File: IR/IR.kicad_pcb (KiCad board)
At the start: 2 copper layers, 209 parts, among them J1 Conn_01x02_Male, J2 Conn_01x10_Female, J3 Conn_01x04_Male, J4 Conn_01x04_Male, Q1 SSM3J332R, Q10 SSM3J332R, Q11 2PB709AR, Q12 2PB709AR, Q13 SSM6K819R, Q14 SSM6K819R, Q15 SSM6K819R, Q16 SSM6K819R, Q2 BSS138, Q3 SSM3J332R, Q4 SSM3J332R, Q5 2PB709AR, Q6 SSM3J332R, Q7 2PB709AR, Q8 SSM3J332R, Q9 2PB709AR, SW1 SW_DIP_x05, SW2 SW_SPDT, SW4 SW_SPST, U1 TSSP58038, U10 TSSP58038, U11 TSSP58038, U12 TSSP58038, U13 TSSP58038, U14 TSSP58038, U15 TSSP58038, U16 TSSP58038, U17 TSSP58038, U18 74HC4051, U19 74HC4051, U2 TSSP58038, U20 STM32C031K4T6, U21 MAX3485, U3 TSSP58038, U4 TSSP58038, U5 AZ1084CD-3.3, U6 TSSP58038, U7 TSSP58038, U8 TSSP58038, U9 TSSP58038

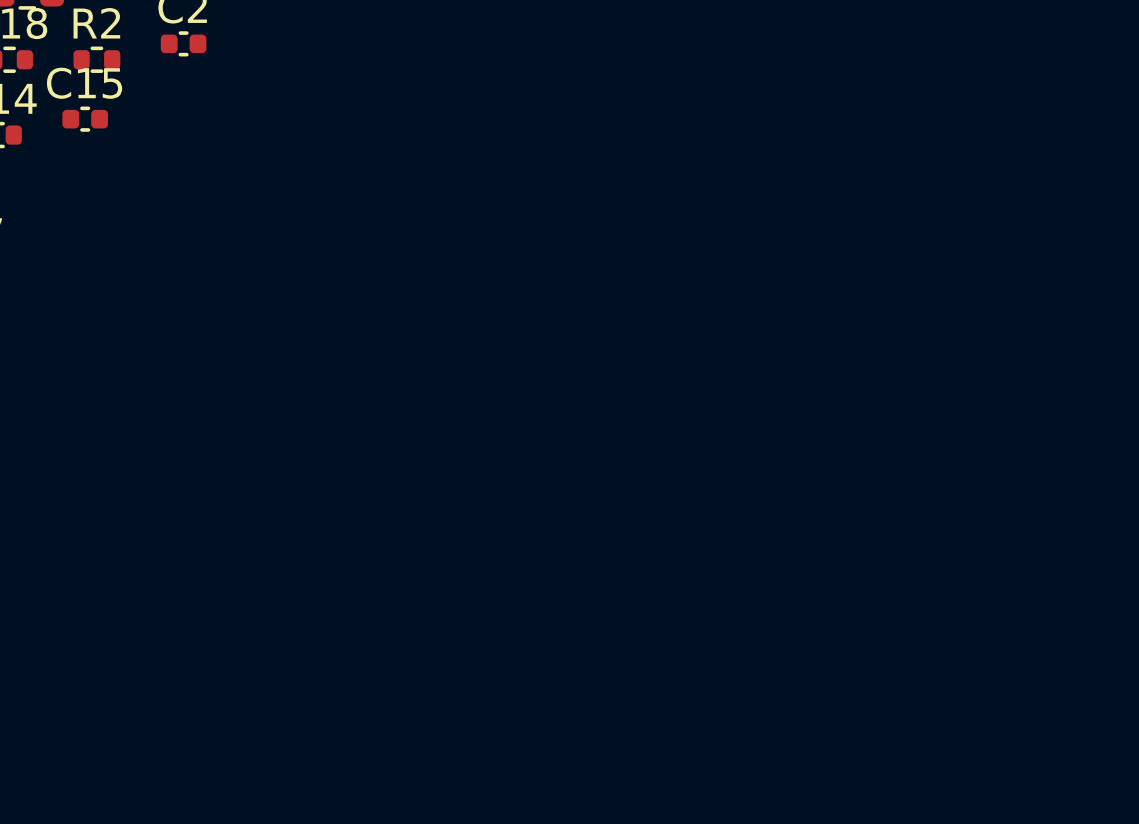
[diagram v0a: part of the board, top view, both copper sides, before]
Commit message: 構成図追加
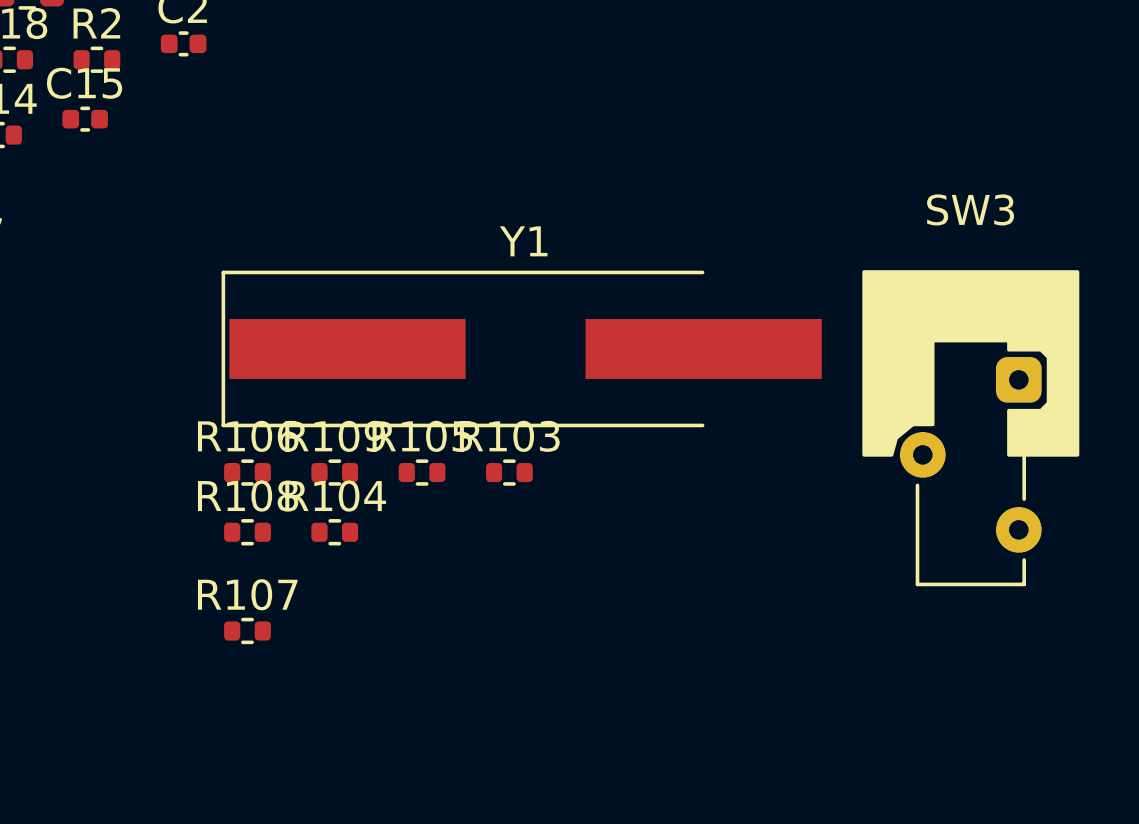
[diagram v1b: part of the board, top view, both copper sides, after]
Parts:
- added R103: 5.1k, Resistor_SMD:R_0402_1005Metric, F.Cu at (168.5, 62.2)
- added R104: 5.1k, Resistor_SMD:R_0402_1005Metric, F.Cu at (162.7, 64.2)
- added R105: 5.1k, Resistor_SMD:R_0402_1005Metric, F.Cu at (165.6, 62.2)
- added R106: 10k, Resistor_SMD:R_0402_1005Metric, F.Cu at (159.8, 62.2)
- added R107: 10k, Resistor_SMD:R_0402_1005Metric, F.Cu at (159.8, 67.5)
- added R108: 10k, Resistor_SMD:R_0402_1005Metric, F.Cu at (159.8, 64.2)
- added R109: 10k, Resistor_SMD:R_0402_1005Metric, F.Cu at (162.7, 62.2)
- added SW3: SW_SPDT_White, Slide_Switch:SW_Slide_SPDT_White, F.Cu at (183.9, 61.7)
- added Y1: 48MHz, Crystal:Crystal_SMD_HC49-SD_HandSoldering, F.Cu at (169.0, 58.1)
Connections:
- R32 pad 1: Mux_OUT0 -> GND
- R32 pad 2: GND -> Mux_OUT0
- R33 pad 1: Mux_OUT1 -> GND
- R33 pad 2: GND -> Mux_OUT1

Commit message: 人力曲面配線中
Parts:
- removed C24: 22pF, Capacitor_SMD:C_0603_1608Metric
- added C30: 0.1uF, Capacitor_SMD:C_0402_1005Metric, B.Cu at (119.5, 113.2)
- added C31: 0.1uF, Capacitor_SMD:C_0402_1005Metric, B.Cu at (120.2, 121.2)
- added U22: NJU6319AE, Package_SO:SOP-8_3.9x4.9mm_P1.27mm, B.Cu at (136.0, 102.8)
- C1, C14: value 4.7uF -> 1uF; footprint Capacitor_SMD:C_0603_1608Metric -> Capacitor_SMD:C_0402_1005Metric; moved to B.Cu
- C10, C11, C12, C13, C15, C16, C17, C18, C19, C2, C20, C21, C22, C25, C26, C29, C3, C4, C5, C6, C7, C8, C9, D10, D11, D7, D8, D9, H1, H2, H3, JP1, Q1, Q10, Q2, Q3, Q4, Q6, Q8, R1, R10, R100, R101, R102, R103, R104, R105, R106, R107, R108, R109, R11, R12, R13, R14, R15, R16, R17, R18, R19, R2, R20, R21, R22, R23, R24, R25, R26, R27, R28, R29, R3, R30, R31, R32, R33, R34, R35, R36, R37, R38, R39, R4, R40, R41, R42, R43, R44, R45, R46, R47, R48, R49, R5, R50, R51, R52, R53, R54, R55, R56, R57, R58, R59, R6, R60, R61, R62, R63, R64, R65, R66, R67, R68, R69, R7, R70, R71, R72, R73, R74, R75, R76, R77, R78, R79, R8, R80, R81, R82, R83, R84, R85, R86, R87, R88, R89, R9, R90, R91, R92, R93, R94, R95, R96, R97, R98, R99, TP1, TP2, TP3, U18, U19, U20, U21, U5: moved to B.Cu
- C23: value 22pF -> 0.1uF; footprint Capacitor_SMD:C_0603_1608Metric -> Capacitor_SMD:C_0402_1005Metric; moved to B.Cu
- D1, D2: value SBR1A40SA -> 1N5819WS; footprint Diode_SMD:D_SMA_Handsoldering -> Diode_SMD:D_SOD-323_HandSoldering; moved to B.Cu
- D12, D13, D14, D15, D16, D17, D18, D19, D20, D21, D22, D23, D24, D25, D26, D27: footprint LED_THT:LED_D3.0mm_Horizontal_O1.27mm_Z2.0mm -> LED_3.0mm_Center:LED_D3.0mm_Horizontal_O1.27mm_Z2.0mm
- J1: footprint Connector_Molex:Molex_SPOX_5268-02A_1x02_P2.50mm_Horizontal -> Connector_Molex:Molex_SPOX_5267-02A_1x02_P2.50mm_Vertical; moved to B.Cu
- J2: value Conn_01x10_Female -> Conn_01x10_Male; footprint Connector_IDC:IDC-Header_2x05_P2.54mm_Horizontal -> BoxHeader_1.27mm:BoxHeader_2x05_P1.27mm_Vertical_SMD
- J3, J4: footprint Connector_Molex:Molex_SPOX_5268-04A_1x04_P2.50mm_Horizontal -> Connector_Molex:Molex_SPOX_5267-04A_1x04_P2.50mm_Vertical; moved to B.Cu
- Q11, Q12, Q5, Q7, Q9: value 2PB709AR -> S8050; footprint Package_TO_SOT_SMD:SC-59_Handsoldering -> Package_TO_SOT_SMD:SOT-23; moved to B.Cu
- Q13, Q14, Q15, Q16: value SSM6K819R -> SSM3K345R; footprint TSOP6F:SSM6J808R -> Package_TO_SOT_SMD:SOT-23W; moved to B.Cu
- Y1: value 48MHz -> 16MHz; footprint Crystal:Crystal_SMD_HC49-SD_HandSoldering -> Crystal:Crystal_SMD_3225-4Pin_3.2x2.5mm_HandSoldering; moved to B.Cu
- moved D24 227.9 mm to (-43.2, 8.57), turned to -78.75 degrees
- moved D21 224.1 mm to (-24.4, -36.6), turned to -146.25 degrees
- moved D23 220.9 mm to (-43.2, -8.60), turned to -101.25 degrees
- moved D22 217.4 mm to (-36.6, -24.5), turned to -123.75 degrees
- moved D26 208.5 mm to (-24.4, 36.6), turned to -33.75 degrees
- moved D25 205.5 mm to (-36.6, 24.4), turned to -56.25 degrees
- moved D20 200.8 mm to (-8.58, -43.2), turned to -168.75 degrees
- moved R74 198.7 mm to (-44.6, -7.25), turned to -101.25 degrees
- moved R85 197.2 mm to (-35.3, -25.4), turned to 56.25 degrees
- moved R82 197.1 mm to (-44.0, -10.2), turned to 78.75 degrees
- moved SW3 196.4 mm to (-11.5, 82.0)
- moved R77 195.2 mm to (-37.0, -22.9), turned to -123.75 degrees
- moved D19 194.6 mm to (8.58, -43.2), turned to 168.75 degrees
- moved R81 193.1 mm to (-36.5, -26.3), turned to 56.25 degrees
- moved R92 188.4 mm to (-38.4, 23.6), turned to 123.75 degrees
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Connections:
- C23 pad 1: GND -> +3.3V
- C23 pad 2: OSC_IN -> GND
- Q13 pad 1: IR_emit0 -> Blightness_Max
- Q13 pad 2: IR_emit0 -> GND
- Q13 pad 3: Blightness_Max -> IR_emit0
- Q14 pad 1: IR_emit1 -> Blightness_2nd
- Q14 pad 2: IR_emit1 -> GND
- Q14 pad 3: Blightness_2nd -> IR_emit1
- Q15 pad 1: IR_emit2 -> Blightness_3rd
- Q15 pad 2: IR_emit2 -> GND
- Q15 pad 3: Blightness_3rd -> IR_emit2
- Q16 pad 1: IR_emit3 -> Blightness_Min
- Q16 pad 2: IR_emit3 -> GND
- Q16 pad 3: Blightness_Min -> IR_emit3
- U20 pad 2: unconnected-(U20-Pad2) -> OSC_IN
- U20 pad 6: unconnected-(U20-Pad6) -> NRST
- Y1 pad 1: OSC_OUT -> Net-(U22-Pad2)
- Y1 pad 2: OSC_IN -> GND
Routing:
- net GND: track 0.00 -> 281.0 mm, vias 0 -> 4
- net +3.3V: track 0.00 -> 258.5 mm
- net IR_rcpt8: track 0.00 -> 112.6 mm
- net VDD: track 0.00 -> 98.5 mm
- net IR_rcpt7: track 0.00 -> 96.8 mm
- net IR_rcpt6: track 0.00 -> 80.2 mm
- net IR_rcpt5: track 0.00 -> 66.9 mm
- net IR_rcpt4: track 0.00 -> 59.0 mm
- net IR_rcpt3: track 0.00 -> 40.8 mm
- net IR_emit1: track 0.00 -> 39.6 mm
- net IR_rcpt2: track 0.00 -> 23.0 mm
- net IR_emit0: track 0.00 -> 21.5 mm
- net Net-(D19-Pad1): track 0.00 -> 6.99 mm
- net Net-(D20-Pad1): track 0.00 -> 5.73 mm
- net Net-(D18-Pad1): track 0.00 -> 5.06 mm
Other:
- board outline added: 96 x 138 mm

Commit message: ゴリ押し人力配線
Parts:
- moved U19 178.8 mm to (-41.5, 57.1), turned to -157.5 degrees
- moved C31 178.4 mm to (-46.3, 57.2), turned to -67.5 degrees
- moved C18 147.3 mm to (-39.1, -15.2), turned to 67.5 degrees
- moved C17 144.8 mm to (-30.4, -29.0), turned to 45 degrees
- moved C19 144.3 mm to (-41.9, 0.70), turned to 90 degrees
- moved C16 137.9 mm to (-16.9, -38.6), turned to 22.5 degrees
- moved C20 137.6 mm to (-38.4, 17.0), turned to 112.5 degrees
- moved C21 126.5 mm to (-29.1, 30.4), turned to 135 degrees
- moved C15 126.2 mm to (-0.79, -42.2), turned to 0 degrees
- moved C12 115.0 mm to (15.3, -39.4), turned to -22.5 degrees
- moved C22 111.9 mm to (-15.4, 39.2), turned to 157.5 degrees
- moved C11 97.9 mm to (29.3, -30.4), turned to -45 degrees
- moved C3 86.7 mm to (0.94, 42.2)
- moved C10 79.8 mm to (38.7, -16.9), turned to -67.5 degrees
- moved C4 70.7 mm to (17.0, 38.7), turned to -157.5 degrees
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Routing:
- net IR_emit2: track 0.00 -> 151.2 mm, vias 0 -> 13
- net IR_emit3: track 0.00 -> 140.8 mm, vias 0 -> 13
- net IR_emit1: track 39.6 -> 177.2 mm, vias 0 -> 13
- net IR_emit0: track 21.5 -> 130.8 mm
- net GND: track 281.0 -> 389.5 mm, vias 4 -> 26
- net IR_rcpt9: track 0.00 -> 98.5 mm
- net +3.3V: track 258.5 -> 356.0 mm
- net IR_rcpt10: track 0.00 -> 83.0 mm
- net IR_rcpt11: track 0.00 -> 69.5 mm
- net IR_rcpt12: track 0.00 -> 62.5 mm
- net IR_rcpt13: track 0.00 -> 51.0 mm
- net IR_rcpt14: track 0.00 -> 28.4 mm
- net IR_rcpt15: track 0.00 -> 12.7 mm
- net IR_rcpt6: track 80.2 -> 87.0 mm
- net IR_rcpt8: track 112.6 -> 118.8 mm
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
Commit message: IR半分
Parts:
- removed C13: ADJ_ST, Capacitor_SMD:C_0603_1608Metric
- removed C14: 1uF, Capacitor_SMD:C_0402_1005Metric
- removed C2: 0.1uF, Capacitor_SMD:C_0402_1005Metric
- removed D10, D9: Green, LED_SMD:LED_0603_1608Metric_Pad1.05x0.95mm_HandSolder
- removed D7: D_Zener, Diode_SMD:D_SOD-323_HandSoldering
- removed H1, H2: MountingHole_Pad, TestPoint:TestPoint_Pad_1.5x1.5mm
- removed Q10, Q4, Q6, Q8: SSM3J332R, Package_TO_SOT_SMD:SOT-23W
- removed Q11, Q5, Q7, Q9: S8050, Package_TO_SOT_SMD:SOT-23
- removed R16, R18, R20, R21, R23, R24, R25, R26, R27: 10k, Resistor_SMD:R_0402_1005Metric
- removed R19, R29, R30: 1k, Resistor_SMD:R_0402_1005Metric
- removed R22: 100k, Resistor_SMD:R_0402_1005Metric
- D11, D8, JP1, Q13, Q14, Q15, Q16: moved to F.Cu
- U20: value STM32C031K4T6 -> STM32G030K6T6
- moved R17 191.0 mm to (7.06, 48.9), turned to 0 degrees
- moved C8 185.9 mm to (7.06, 49.9)
- moved C7 184.1 mm to (12.7, 55.0)
- moved R28 182.1 mm to (17.2, 58.3)
- moved D2 181.5 mm to (10.1, 49.4)
- moved U5 181.4 mm to (8.65, 56.0), turned to -90 degrees
- moved C27 174.2 mm to (12.2, 58.9), turned to -90 degrees
- moved C29 172.3 mm to (-16.2, 74.6), turned to -90 degrees
- moved U21 171.4 mm to (-12.9, 70.8), turned to -90 degrees
- moved C28 170.4 mm to (3.29, 59.0), turned to -90 degrees
- moved R38 168.8 mm to (-16.2, 72.5), turned to 90 degrees
- moved JP1 168.6 mm to (-18.7, 75.0)
- moved R37 167.2 mm to (-14.0, 75.1)
- moved Q12 167.0 mm to (-13.3, 65.0), turned to -90 degrees
- moved R35 166.7 mm to (-15.7, 65.9), turned to 90 degrees
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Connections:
- C8 pad 1: /3.3VSYS -> +3.3V
- D2 pad 2: /3.3VSYS -> +3.3V
- J2 pad 1: /3.3VBUS -> unconnected-(J2-Pad1)
- R17 pad 2: /3.3VSYS -> +3.3V
- U20 pad 1: unconnected-(U20-Pad1) -> LED1
- U20 pad 10: unconnected-(U20-Pad10) -> Mux_IN2
- U20 pad 11: unconnected-(U20-Pad11) -> Mux_IN1
- U20 pad 12: unconnected-(U20-Pad12) -> Mux_IN0
- U20 pad 13: unconnected-(U20-Pad13) -> Blightness_Max
- U20 pad 14: unconnected-(U20-Pad14) -> Blightness_2nd
- U20 pad 15: unconnected-(U20-Pad15) -> Blightness_3rd
- U20 pad 16: unconnected-(U20-Pad16) -> Blightness_Min
- U20 pad 19: unconnected-(U20-Pad19) -> MainTX_STLinkRX
- U20 pad 20: unconnected-(U20-Pad20) -> Slide_SW0
- U20 pad 21: unconnected-(U20-Pad21) -> MainRX_STLinkTX
- U20 pad 22: unconnected-(U20-Pad22) -> DIP_SW4
- U20 pad 23: unconnected-(U20-Pad23) -> DIP_SW3
- U20 pad 24: unconnected-(U20-Pad24) -> TMS
- U20 pad 25: unconnected-(U20-Pad25) -> TCK
- U20 pad 26: unconnected-(U20-Pad26) -> MainRX_RS485TX
- U20 pad 27: unconnected-(U20-Pad27) -> DIP_SW2
- U20 pad 28: unconnected-(U20-Pad28) -> DIP_SW1
- U20 pad 29: unconnected-(U20-Pad29) -> DIP_SW0
- U20 pad 30: unconnected-(U20-Pad30) -> LED0
- U20 pad 31: unconnected-(U20-Pad31) -> MonitorLED0
- U20 pad 32: unconnected-(U20-Pad32) -> LED2
- U20 pad 7: unconnected-(U20-Pad7) -> Mux_OUT1
- U20 pad 8: unconnected-(U20-Pad8) -> Mux_OUT0
- U20 pad 9: unconnected-(U20-Pad9) -> MainTX_RS485RX
- U5 pad 2: /3.3VSYS -> +3.3V
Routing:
- net +3.3V: track 356.0 -> 595.4 mm, vias 0 -> 23
- net VDD: track 95.5 -> 329.1 mm, vias 0 -> 27
- net IR_emit0: track 130.8 -> 348.9 mm, vias 0 -> 2
- net IR_emit2: track 151.2 -> 369.2 mm, vias 13 -> 33
- net IR_emit1: track 177.2 -> 394.3 mm, vias 13 -> 31
- net GND: track 389.5 -> 598.4 mm, vias 26 -> 177
- net IR_emit3: track 140.8 -> 339.4 mm, vias 13 -> 32
- net DIP_SW4: track 0.00 -> 38.2 mm
- net NRST: track 0.00 -> 36.7 mm, vias 0 -> 3
- net Mux_IN0: track 0.00 -> 35.7 mm, vias 0 -> 2
- net Mux_IN1: track 0.00 -> 34.4 mm, vias 0 -> 2
- net DIP_SW3: track 0.00 -> 34.3 mm
- net Mux_IN2: track 0.00 -> 33.4 mm, vias 0 -> 2
- net RS485_A: track 0.00 -> 32.9 mm
- net RS485_B: track 0.00 -> 31.5 mm
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- added copper zone on B.Cu, net /5VBAT
- added copper zone on B.Cu, net /S-S
- added copper zone on B.Cu, net GND
- added copper zone on F.Cu, net GND
- added copper zone on B.Cu, net VDD
- added copper zone on F.Cu, net VDD

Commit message: LargeMDほぼ完成
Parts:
- H3: moved to F.Cu
- moved C1 158.7 mm to (154.3, 131.3)
- moved C11 158.7 mm to (166.7, 48.8)
- moved C12 158.7 mm to (152.8, 39.9)
- moved C15 158.7 mm to (136.7, 37.1)
- moved C16 158.7 mm to (120.6, 40.6)
- moved C17 158.7 mm to (107.0, 50.2)
- moved C18 158.7 mm to (98.4, 64.1)
- moved C20 158.7 mm to (98.8, 96.4)
- moved C21 158.7 mm to (108.3, 109.8)
- moved C22 158.7 mm to (122.1, 118.5)
- moved C25 158.7 mm to (140.5, 148.2)
- moved C27 158.7 mm to (149.7, 138.2)
- moved C28 158.7 mm to (140.8, 138.2)
- moved C3 158.7 mm to (138.4, 121.5)
- moved C30 158.7 mm to (133.6, 128.6)
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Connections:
- net MainRX_RS485TX renamed MainRX2_RS485TX
- net MainRX_STLinkTX renamed MainRX1_STLinkTX
- net MainTX_RS485RX renamed MainTX2_RS485RX
- net MainTX_STLinkRX renamed MainTX1_STLinkRX
- U22 pad 6: Net-(U22-Pad6) -> unconnected-(U22-Pad6)
- U22 pad 7: Net-(U22-Pad6) -> unconnected-(U22-Pad7)
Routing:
- net GND: track 598.4 -> 701.0 mm, vias 177 -> 233
- net 主電源スイッチ: track 2.20 -> 86.5 mm, vias 0 -> 2
- net /S-S: track 4.47 -> 86.7 mm
- net +3.3V: track 595.4 -> 577.1 mm, vias 23 -> 22
- net VDD: track 329.1 -> 336.8 mm
- net NRST: track 36.7 -> 39.8 mm
- net Net-(U22-Pad6): track 1.27 -> 0.00 mm
- net Net-(D6-Pad2): track 1.35 -> 0.52 mm
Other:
- outline, holes or cut-outs redrawn
- board text added: "Designed by @cat_nekonekone"
- board text added: "Tomoshibi"
- board text added: "燈"

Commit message: 製造ファイル出力
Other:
- board text added: "3.3V"
- board text added: "GND"
- board text added: "JLCJLCJLCJLC"
- board text added: "NRST"
- board text added: "PA11"
- board text added: "PA12"
- board text added: "PB3"
- board text added: "PB4"
- board text added: "PB5"
- board text added: "PB6"
- board text added: "PB7"
- board text added: "PB8"
- board text added: "PB9"
- board text added: "PC6"
- board text added: "POWER"
- board text added: "RX1:PA10"
- board text added: "RX2:PA15"
- board text added: "TX1:PA9"
- board text added: "TX2:PA2"
- board text added: "VDD"
- board text added: "[RS485]"
- board text added: "[STLink]"
